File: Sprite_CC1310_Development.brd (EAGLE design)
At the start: 50 x 50 mm, 68 parts, among them U1 NCP1402

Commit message: need new boost converter, obsolete component :(
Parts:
- removed COAX, COAX1: 734120110, con-coax:734120110
- added R18: 10k, SparkFun:0402-RES
- added U$3, U$7: MM5329-2700, MM5329-2700:MM5829-2700
- added U$8: L6920, L6920:L6920
- L1, L3: device SparkFun:C0402 -> SparkFun:0603
- moved C19 1.95 mm to (32.2, 23.8), turned to 270 degrees
- moved C8 0.87 mm to (30.0, 23.8)
- moved C7 0.87 mm to (31.1, 23.8)
- moved L1 0.57 mm to (31.9, 21.2)
- moved L3 0.50 mm to (34.4, 23.7)
- moved C9 0.35 mm to (29.0, 23.8)
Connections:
- new net N$40: U$8.1, U$8.8
- new net N$41: R18.1, U$8.5
- net GND: now also U$3.GND1, U$3.GND2, U$3.GND3, U$7.GND1, U$7.GND2, U$7.GND3, U$8.6; no longer COAX.S@1, COAX.S@2, COAX.S@3, COAX1.S@1, COAX1.S@2, COAX1.S@3
- net N$14: now also U$7.SIG; no longer COAX1.1
- net N$26: now also U$3.SIG; no longer COAX.1
- net SOLAR_CELLS: now also R18.2
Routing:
- net N$26: track 5.66 -> 8.69 mm
- net VDDR: track 20.9 -> 22.4 mm
- net GND: track 220.3 -> 219.3 mm
- net SOLAR_CELLS: track 23.4 -> 24.3 mm

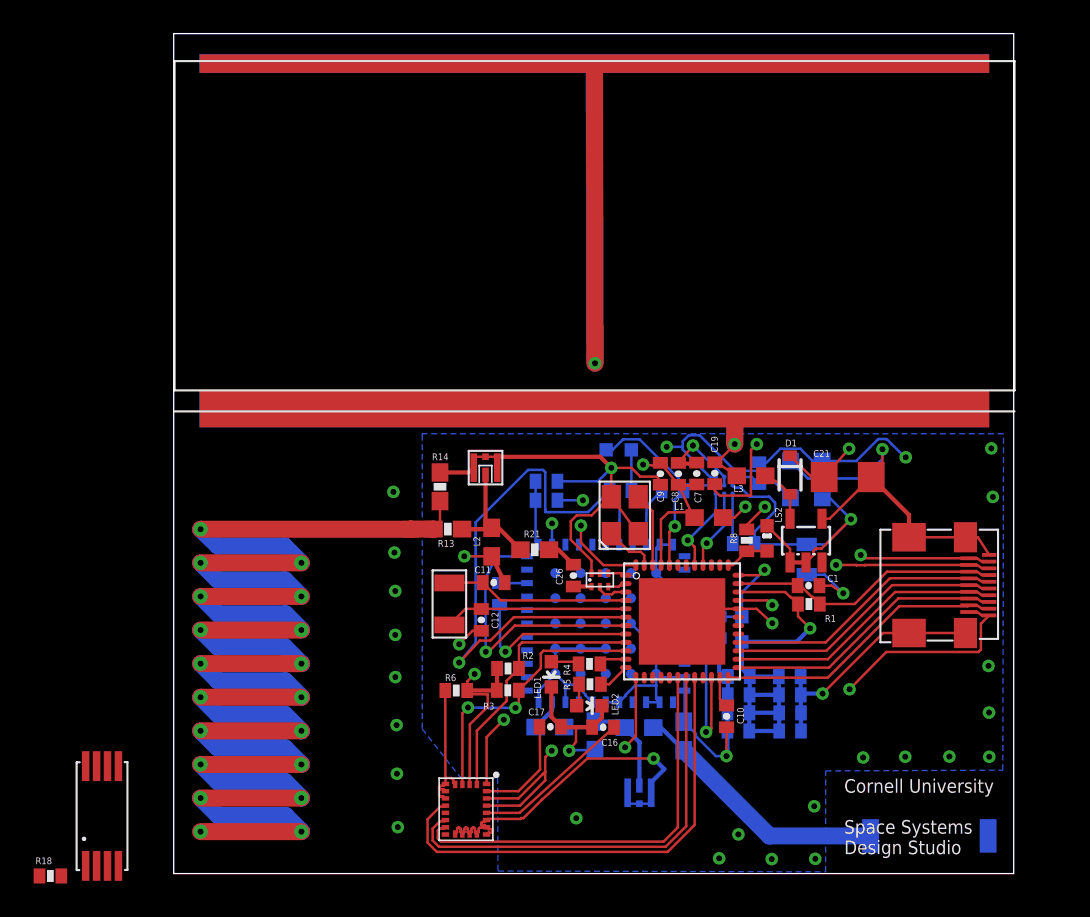
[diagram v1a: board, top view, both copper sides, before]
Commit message: updated boost regulator
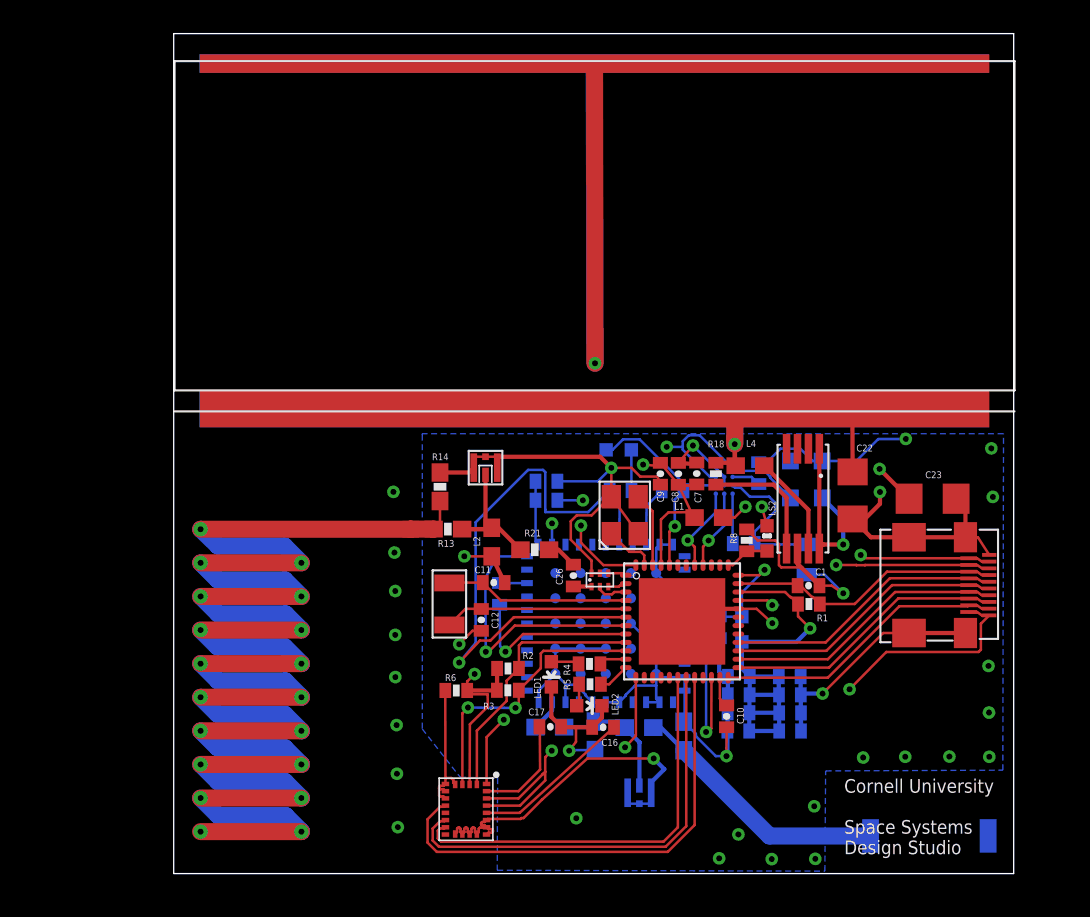
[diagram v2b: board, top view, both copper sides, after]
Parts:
- removed C19: 10 uF, SparkFun:0402-CAP
- removed C21: 68 uF, SparkFun:1206
- removed D1: MBRA140, SparkFun:SOD-323
- removed L3: 47uH, SparkFun:0603
- removed U1: NCP1402, SparkFun:SOT23-5
- added C22, C23: 47 uF, SparkFun:1206
- added L4: 47uH, SparkFun:0603
- moved R18 46.3 mm to (32.3, 23.8), turned to 90 degrees
- moved U$8 45.8 mm to (37.5, 22.3), turned to 180 degrees
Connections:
- removed net N$16: D1.2, L3.2, U1.5
- removed net N$40: U$8.1, U$8.8
- new net N$48: L4.1, U$8.7
- net GND: now also C22.2, C23.2; no longer C19.2, C21.2, U1.4
- net SOLAR_CELLS: now also C22.1, L4.2; no longer C19.1, L3.1
- net VDDS: now also C23.1, U$8.1, U$8.8; no longer C21.1, D1.1, U1.1, U1.2
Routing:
- net SOLAR_CELLS: track 24.3 -> 34.9 mm
- net GND: track 219.3 -> 210.6 mm, vias 14 -> 12
- net N$41: track 0.00 -> 7.56 mm
- net N$48: track 0.00 -> 6.03 mm
- net N$16: track 3.32 -> 0.00 mm
- net COIL: track 1352.2 -> 1352.9 mm
- net VDDS: track 127.2 -> 127.3 mm, vias 12 -> 13

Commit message: BOM
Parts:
- C22, C23: device SparkFun:1206 -> SparkFun:0805
- moved C10 1.20 mm to (33.7, 10.3), turned to 0 degrees
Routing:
- net VDDS: track 127.3 -> 126.1 mm
- net N$48: track 6.03 -> 5.03 mm
- net N$41: track 7.56 -> 6.57 mm
- net VDDR: track 22.4 -> 21.6 mm
- net GND: track 210.6 -> 210.1 mm, vias 12 -> 13

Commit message: cleaning up
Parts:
- renumbered SER3635CT-ND to TSX3225
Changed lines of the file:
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@@
 </element>
 <element name="REAR_PANEL" library="ALTA_CELL" package="ALTA_CELL" value="ALTA_CELL" x="25.052265625" y="38.562209375" rot="R180"/>
-<element name="SER3635CT-ND" library="TSX-3225" package="TSX-3225" value="TSX-3225" x="26.85" y="21.33" rot="R90"/>
+<element name="TSX3225" library="TSX-3225" package="TSX-3225" value="TSX-3225" x="26.85" y="21.33" rot="R90"/>
 <element name="U$2" library="LV8417CS" package="LV8417CS" value="LV8417CS" x="32.77" y="23.11" rot="MR0"/>
 <element name="U$4" library="Panasonic_Rectifier" package="PANASONIC_RECTIFIER" value="PANASONIC_RECTIFIER" x="37.66" y="23.46" smashed="yes" rot="MR0"/>
@@
 <contactref element="C11" pad="2"/>
 <contactref element="C12" pad="2"/>
-<contactref element="SER3635CT-ND" pad="2"/>
-<contactref element="SER3635CT-ND" pad="4"/>
+<contactref element="TSX3225" pad="2"/>
+<contactref element="TSX3225" pad="4"/>
 <contactref element="LED1" pad="C"/>
 <contactref element="LED2" pad="C"/>
@@
 <signal name="X24M_N">
 <contactref element="MICROCONTROLLER" pad="46"/>
-<contactref element="SER3635CT-ND" pad="3"/>
+<contactref element="TSX3225" pad="3"/>
 <wire x1="27.65" y1="22.43" x2="28.51" y2="21.57" width="0.1524" layer="1"/>
 <wire x1="28.51" y1="21.57" x2="28.51" y2="18.36" width="0.1524" layer="1"/>
@@
 <signal name="X24M_P">
 <contactref element="MICROCONTROLLER" pad="47"/>
-<contactref element="SER3635CT-ND" pad="1"/>
+<contactref element="TSX3225" pad="1"/>
 <wire x1="28.01" y1="18.36" x2="28.01" y2="18.95011875" width="0.1524" layer="1"/>
 <wire x1="28.01" y1="18.95011875" x2="27.8064125" y2="19.15370625" width="0.1524" layer="1"/>

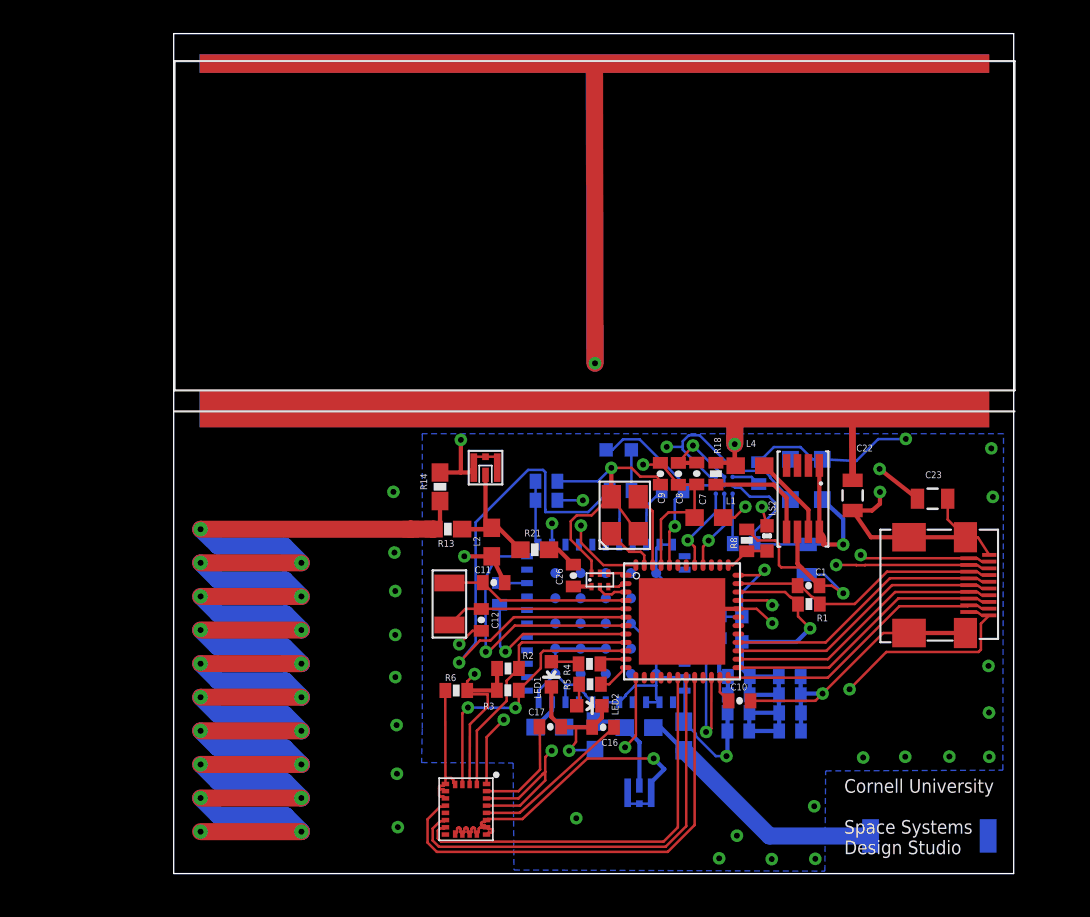
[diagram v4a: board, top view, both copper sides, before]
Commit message: Updated matching network
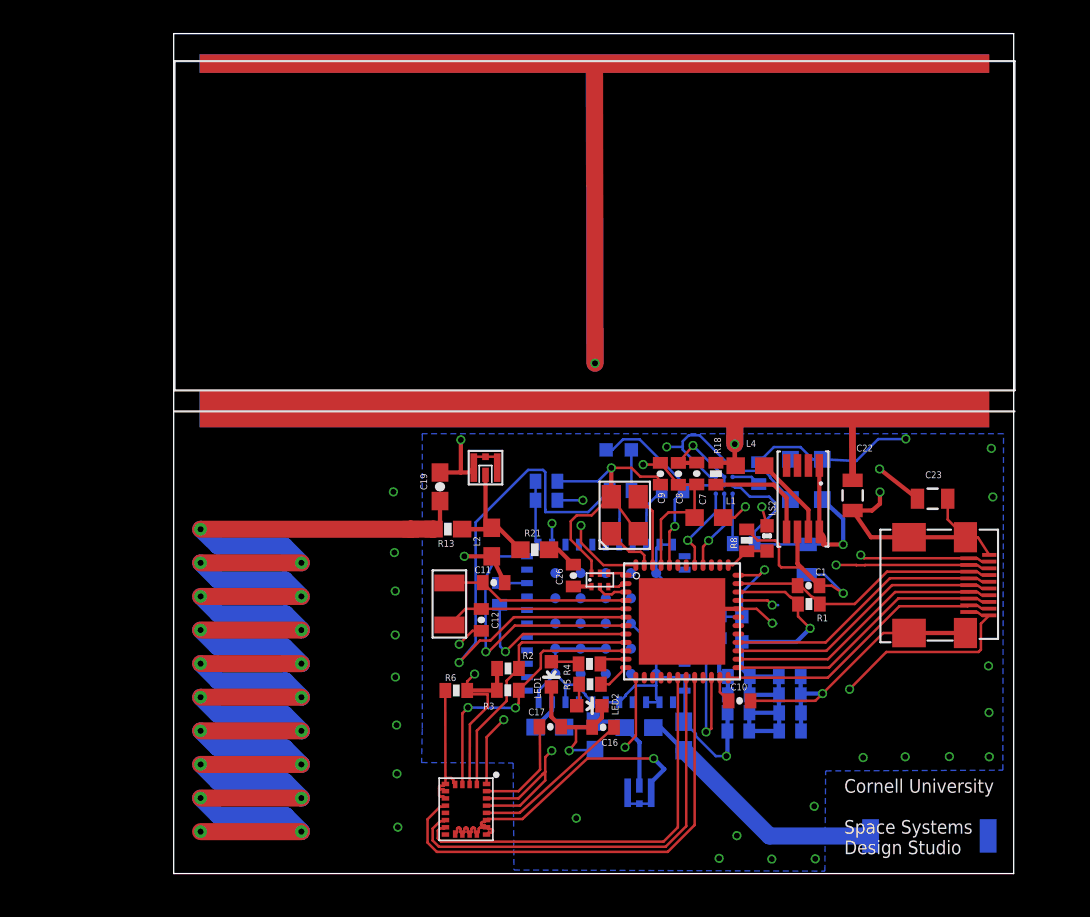
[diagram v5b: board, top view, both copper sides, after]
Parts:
- removed R14, R16: 0, SparkFun:0603-RES
- added C19: 104 pF, SparkFun:0603-CAP
- added L3: 2.2 nH, SparkFun:0603
- L2: value 5.6 nH -> DNP
- R17: value 0 -> DNP
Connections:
- net ANTENNA: now also C19.2; no longer R14.2
- net GND: now also C19.1, L3.1; no longer R14.1, R16.1
- net N$15: now also L3.2; no longer R16.2
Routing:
- net VDDS: track 126.1 -> 124.6 mm
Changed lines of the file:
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@@
 </class>
 </classes>
-<designrules name="default *">
-<description language="de">&lt;b&gt;EAGLE Design Rules&lt;/b&gt;
+<designrules name="oshpark-4layer">
+<description language="en">&lt;b&gt;OSH Park Design Rules&lt;/b&gt;
 &lt;p&gt;
-Die Standard-Design-Rules sind so gewählt, dass sie für
-die meisten Anwendungen passen. Sollte ihre Platine
-besondere Anforderungen haben, treffen Sie die erforderlichen
-Einstellungen hier und speichern die Design Rules unter
-einem neuen Namen ab.</description>
-<description language="en">&lt;b&gt;EAGLE Design Rules&lt;/b&gt;
+Please make sure your boards conform to these design rules.
+&lt;/p&gt;
 &lt;p&gt;
-The default Design Rules have been set to cover
-a wide range of applications. Your particular design
-may have different requirements, so please make the
-necessary adjustments and save your customized
-design rules under a new name.</description>
+Note, that not all DRC settings must be set by the manufacturer. Several can be adjusted for the design, including those listed on our docs page here.
+&lt;a href=&quot;http://docs.oshpark.com/design-tools/eagle/design-rules-files/&quot;&gt;Adjustable Settings&lt;/a&gt;
+&lt;/p&gt;</description>
 <param name="layerSetup" value="(1*2*15*16)"/>
-<param name="mtCopper" value="0.035mm 0.035mm 0.035mm 0.035mm 0.035mm 0.035mm 0.035mm 0.035mm 0.035mm 0.035mm 0.035mm 0.035mm 0.035mm 0.035mm 0.035mm 0.035mm"/>
-<param name="mtIsolate" value="1.5mm 0.15mm 0.2mm 0.15mm 0.2mm 0.15mm 0.2mm 0.15mm 0.2mm 0.15mm 0.2mm 0.15mm 0.2mm 0.15mm 0.2mm"/>
-<param name="mdWireWire" value="6mil"/>
-<param name="mdWirePad" value="6mil"/>
-<param name="mdWireVia" value="6mil"/>
-<param name="mdPadPad" value="6mil"/>
-<param name="mdPadVia" value="6mil"/>
-<param name="mdViaVia" value="6mil"/>
-<param name="mdSmdPad" value="6mil"/>
-<param name="mdSmdVia" value="6mil"/>
-<param name="mdSmdSmd" value="6mil"/>
-<param name="mdViaViaSameLayer" value="6mil"/>
+<param name="mtCopper" value="0.035559375mm 0.01778125mm 0.0356mm 0.0356mm 0.0356mm 0.0356mm 0.0356mm 0.0356mm 0.0356mm 0.0356mm 0.0356mm 0.0356mm 0.0356mm 0.0356mm 0.01778125mm 0.035559375mm"/>
+<param name="mtIsolate" value="0.17018125mm 47mil 0.2007mm 0.1499mm 0.2007mm 0.1499mm 0.2007mm 0.1499mm 0.2007mm 0.1499mm 0.2007mm 0.1499mm 0.2007mm 0.1499mm 0.17018125mm"/>
+<param name="mdWireWire" value="5mil"/>
+<param name="mdWirePad" value="5mil"/>
+<param name="mdWireVia" value="5mil"/>
+<param name="mdPadPad" value="5mil"/>
+<param name="mdPadVia" value="5mil"/>
+<param name="mdViaVia" value="5mil"/>
+<param name="mdSmdPad" value="5mil"/>
+<param name="mdSmdVia" value="5mil"/>
+<param name="mdSmdSmd" value="5mil"/>
+<param name="mdViaViaSameLayer" value="8mil"/>
 <param name="mnLayersViaInSmd" value="2"/>
-<param name="mdCopperDimension" value="40mil"/>
+<param name="mdCopperDimension" value="15mil"/>
 <param name="mdDrill" value="6mil"/>
 <param name="mdSmdStop" value="0mil"/>
-<param name="msWidth" value="6mil"/>
-<param name="msDrill" value="0.35mm"/>
-<param name="msMicroVia" value="9.99mm"/>
+<param name="msWidth" value="5mil"/>
+<param name="msDrill" value="10mil"/>
+<param name="msMicroVia" value="10mil"/>
 <param name="msBlindViaRatio" value="0.5"/>
 <param name="rvPadTop" value="0.25"/>
@@
 <param name="rvMicroViaOuter" value="0.25"/>
 <param name="rvMicroViaInner" value="0.25"/>
-<param name="rlMinPadTop" value="10mil"/>
+<param name="rlMinPadTop" value="4mil"/>
 <param name="rlMaxPadTop" value="20mil"/>
-<param name="rlMinPadInner" value="10mil"/>
+<param name="rlMinPadInner" value="4mil"/>
 <param name="rlMaxPadInner" value="20mil"/>
-<param name="rlMinPadBottom" value="10mil"/>
+<param name="rlMinPadBottom" value="4mil"/>
 <param name="rlMaxPadBottom" value="20mil"/>
-<param name="rlMinViaOuter" value="8mil"/>
+<param name="rlMinViaOuter" value="4mil"/>
 <param name="rlMaxViaOuter" value="20mil"/>
-<param name="rlMinViaInner" value="8mil"/>
+<param name="rlMinViaInner" value="4mil"/>
 <param name="rlMaxViaInner" value="20mil"/>
 <param name="rlMinMicroViaOuter" value="4mil"/>
@@
 <param name="mvStopFrame" value="1"/>
 <param name="mvCreamFrame" value="0"/>
-<param name="mlMinStopFrame" value="4mil"/>
-<param name="mlMaxStopFrame" value="4mil"/>
+<param name="mlMinStopFrame" value="2.5mil"/>
+<param name="mlMaxStopFrame" value="2.5mil"/>
 <param name="mlMinCreamFrame" value="0mil"/>
 <param name="mlMaxCreamFrame" value="0mil"/>
@@
 <attribute name="NAME" x="33.464040625" y="22.389075" size="0.4064" layer="25" rot="R180"/>
 </element>
-<element name="L2" library="SparkFun" package="0603" value="5.6 nH" x="18.93075625" y="19.73369375" smashed="yes" rot="R270">
+<element name="L2" library="SparkFun" package="0603" value="DNP" x="18.93075625" y="19.73369375" smashed="yes" rot="R270">
 <attribute name="NAME" x="18.246575" y="19.48036875" size="0.4064" layer="25" font="vector" rot="R90"/>
 </element>
@@
 <attribute name="NAME" x="16.70680625" y="19.855103125" size="0.4064" layer="25" font="vector" rot="R180"/>
 </element>
-<element name="R14" library="SparkFun" package="0603-RES" value="0" x="15.85185" y="23.02530625" smashed="yes" rot="R270">
+<element name="C19" library="SparkFun" package="0603-CAP" value="104 pF" x="15.85185" y="23.02530625" smashed="yes" rot="R270">
 <attribute name="NAME" x="14.6804875" y="23.817315625" size="0.4064" layer="25" font="vector" rot="R270"/>
 </element>
@@
 <attribute name="NAME" x="28.131415625" y="9.236678125" size="0.4064" layer="26" font="vector" rot="MR0"/>
 </element>
-<element name="R16" library="SparkFun" package="0603-RES" value="0" x="30.36" y="8.19" smashed="yes" rot="MR270">
+<element name="L3" library="SparkFun" package="0603" value="2.2 nH" x="30.36" y="8.19" smashed="yes" rot="MR270">
 <attribute name="NAME" x="31.4126125" y="9.804846875" size="0.4064" layer="26" font="vector" rot="MR270"/>
 </element>
-<element name="R17" library="SparkFun" package="0603-RES" value="0" x="25.08" y="8.2" smashed="yes" rot="MR270">
+<element name="R17" library="SparkFun" package="0603-RES" value="DNP" x="25.08" y="8.2" smashed="yes" rot="MR270">
 <attribute name="NAME" x="24.615675" y="6.591790625" size="0.4064" layer="26" font="vector" rot="MR180"/>
 </element>
@@
 <contactref element="BALUN" pad="6"/>
 <contactref element="L2" pad="2"/>
-<contactref element="R14" pad="1"/>
-<contactref element="R16" pad="1"/>
+<contactref element="C19" pad="1"/>
+<contactref element="L3" pad="1"/>
 <contactref element="R17" pad="2"/>
 <contactref element="U$4" pad="GND"/>
@@
 <wire x1="26.867534375" y1="7.515665625" x2="26.863128125" y2="7.282653125" width="0.1524" layer="15"/>
 <via x="26.867534375" y="7.515665625" extent="1-16" drill="0.35"/>
-<wire x1="39.85148125" y1="19.5881" x2="40.584746875" y2="21.075834375" width="0.1524" layer="15"/>
+<wire x1="39.85148125" y1="19.5881" x2="39.9526" y2="19.713403125" width="0.1524" layer="15"/>
 <via x="39.85148125" y="19.5881" extent="1-16" drill="0.35"/>
 <wire x1="33.82" y1="13.79" x2="37.0741125" y2="13.79" width="0.254" layer="16"/>
@@
 <signal name="N$15">
 <contactref element="R15" pad="1"/>
-<contactref element="R16" pad="2"/>
+<contactref element="L3" pad="2"/>
 <contactref element="U$5" pad="SIG"/>
 <wire x1="28.55" y1="8.69" x2="29.01" y2="8.69" width="0.1524" layer="16"/>
@@
 <wire x1="1.601209375" y1="20.4966625" x2="14.101209375" y2="20.4966625" width="1.016" layer="1"/>
 <contactref element="R13" pad="2"/>
-<contactref element="R14" pad="2"/>
+<contactref element="C19" pad="2"/>
 <wire x1="15.5029625" y1="20.538084375" x2="15.85185" y2="20.886971875" width="0.1524" layer="1"/>
 <wire x1="15.85185" y1="20.886971875" x2="15.85185" y2="22.17530625" width="0.254" layer="1"/>
